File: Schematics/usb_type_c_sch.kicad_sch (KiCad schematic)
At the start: 4 parts, among them J3 USB_C_Receptacle

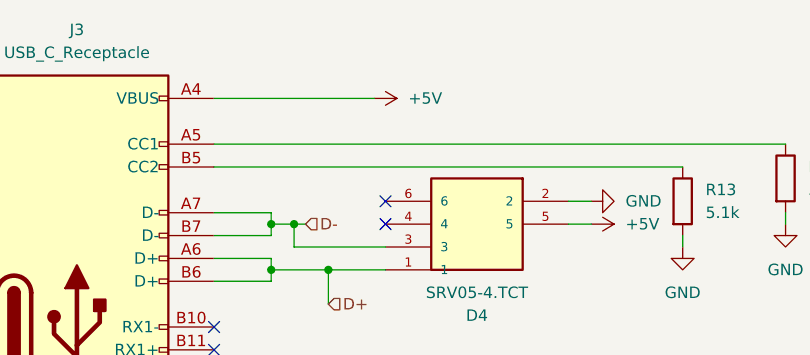
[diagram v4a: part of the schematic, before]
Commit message: finished pin assignments and ran ERC all good ready for layout
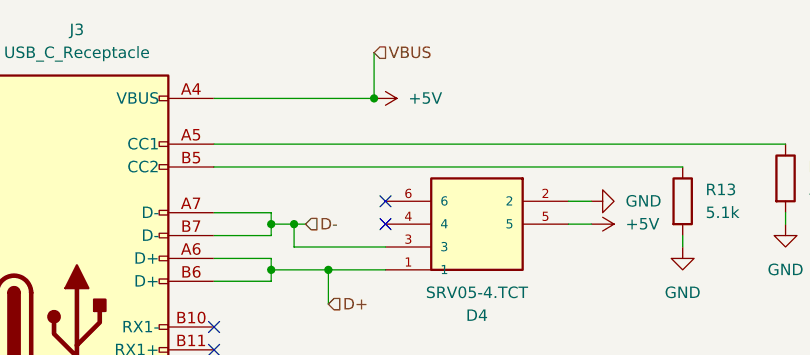
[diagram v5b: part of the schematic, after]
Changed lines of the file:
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@@
+	)
+	(junction
+		(at 140.97 57.15)
+		(diameter 0)
+		(color 0 0 0 0)
 	)
 	(junction
@@
 		(pts
 			(xy 104.14 124.46) (xy 107.95 124.46)
+		)
+		(stroke
+			(width 0)
+			(type default)
+		)
+	)
+	(wire
+		(pts
+			(xy 140.97 52.07) (xy 140.97 57.15)
 		)
 		(stroke
@@
 		(shape input)
 		(at 135.89 80.01 0)
+		(effects
+			(font
+				(size 1.27 1.27)
+			)
+			(justify left)
+		)
+	)
+	(hierarchical_label "VBUS"
+		(shape input)
+		(at 140.97 52.07 0)
 		(effects
 			(font
@@
 			)
 		)
+		(property "Description_1" ""
+			(at 107.95 82.55 0)
+			(effects
+				(font
+					(size 1.27 1.27)
+				)
+				(hide yes)
+			)
+		)
+		(property "MF" ""
+			(at 107.95 82.55 0)
+			(effects
+				(font
+					(size 1.27 1.27)
+				)
+				(hide yes)
+			)
+		)
+		(property "MP" ""
+			(at 107.95 82.55 0)
+			(effects
+				(font
+					(size 1.27 1.27)
+				)
+				(hide yes)
+			)
+		)
+		(property "Package" ""
+			(at 107.95 82.55 0)
+			(effects
+				(font
+					(size 1.27 1.27)
+				)
+				(hide yes)
+			)
+		)
+		(property "Price" ""
+			(at 107.95 82.55 0)
+			(effects
+				(font
+					(size 1.27 1.27)
+				)
+				(hide yes)
+			)
+		)
+		(property "Purchase-URL" ""
+			(at 107.95 82.55 0)
+			(effects
+				(font
+					(size 1.27 1.27)
+				)
+				(hide yes)
+			)
+		)
 		(pin "S1"
 		)
@@
 			)
 		)
+		(property "Description_1" ""
+			(at 162.56 73.66 0)
+			(effects
+				(font
+					(size 1.27 1.27)
+				)
+				(hide yes)
+			)
+		)
+		(property "MF" ""
+			(at 162.56 73.66 0)
+			(effects
+				(font
+					(size 1.27 1.27)
+				)
+				(hide yes)
+			)
+		)
+		(property "MP" ""
+			(at 162.56 73.66 0)
+			(effects
+				(font
+					(size 1.27 1.27)
+				)
+				(hide yes)
+			)
+		)
+		(property "Package" ""
+			(at 162.56 73.66 0)
+			(effects
+				(font
+					(size 1.27 1.27)
+				)
+				(hide yes)
+			)
+		)
+		(property "Price" ""
+			(at 162.56 73.66 0)
+			(effects
+				(font
+					(size 1.27 1.27)
+				)
+				(hide yes)
+			)
+		)
+		(property "Purchase-URL" ""
+			(at 162.56 73.66 0)
+			(effects
+				(font
+					(size 1.27 1.27)
+				)
+				(hide yes)
+			)
+		)
 		(pin "4"
 		)
@@
 			)
 		)
+		(property "Description_1" ""
+			(at 186.69 66.04 0)
+			(effects
+				(font
+					(size 1.27 1.27)
+				)
+				(hide yes)
+			)
+		)
+		(property "MF" ""
+			(at 186.69 66.04 0)
+			(effects
+				(font
+					(size 1.27 1.27)
+				)
+				(hide yes)
+			)
+		)
+		(property "MP" ""
+			(at 186.69 66.04 0)
+			(effects
+				(font
+					(size 1.27 1.27)
+				)
+				(hide yes)
+			)
+		)
+		(property "Package" ""
+			(at 186.69 66.04 0)
+			(effects
+				(font
+					(size 1.27 1.27)
+				)
+				(hide yes)
+			)
+		)
+		(property "Price" ""
+			(at 186.69 66.04 0)
+			(effects
+				(font
+					(size 1.27 1.27)
+				)
+				(hide yes)
+			)
+		)
+		(property "Purchase-URL" ""
+			(at 186.69 66.04 0)
+			(effects
+				(font
+					(size 1.27 1.27)
+				)
+				(hide yes)
+			)
+		)
 		(pin "2"
 		)
@@
 			(at 175.26 68.58 0)
 			(effects
+				(font
+					(size 1.27 1.27)
+				)
+				(hide yes)
+			)
+		)
+		(property "Description_1" ""
+			(at 175.26 68.58 0)
+			(effects
+				(font
+					(size 1.27 1.27)
+				)
+				(hide yes)
+			)
+		)
+		(property "MF" ""
+			(at 175.26 68.58 0)
+			(effects
+				(font
+					(size 1.27 1.27)
+				)
+				(hide yes)
+			)
+		)
+		(property "MP" ""
+			(at 175.26 68.58 0)
+			(effects
+				(font
+					(size 1.27 1.27)
+				)
+				(hide yes)
+			)
+		)
+		(property "Package" ""
+			(at 175.26 68.58 0)
+			(effects
+				(font
+					(size 1.27 1.27)
+				)
+				(hide yes)
+			)
+		)
+		(property "Price" ""
+			(at 175.26 68.58 0)
+			(effects
+				(font
+					(size 1.27 1.27)
+				)
+				(hide yes)
+			)
+		)
+		(property "Purchase-URL" ""
+			(at 175.26 68.58 0)
+			(effects

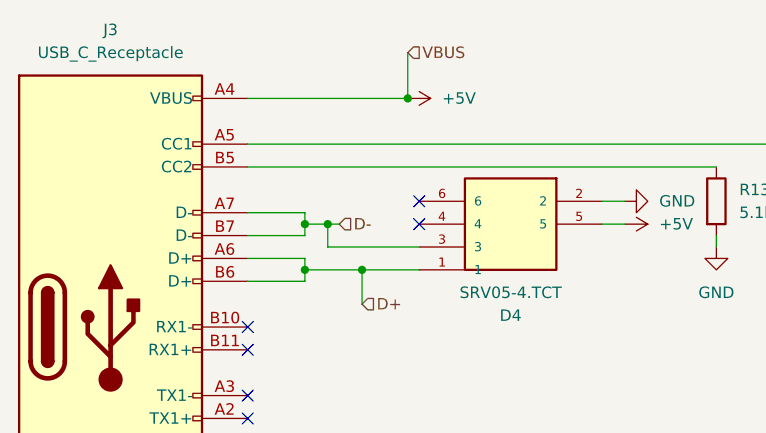
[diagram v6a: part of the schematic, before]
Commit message: began routing, need layout approval
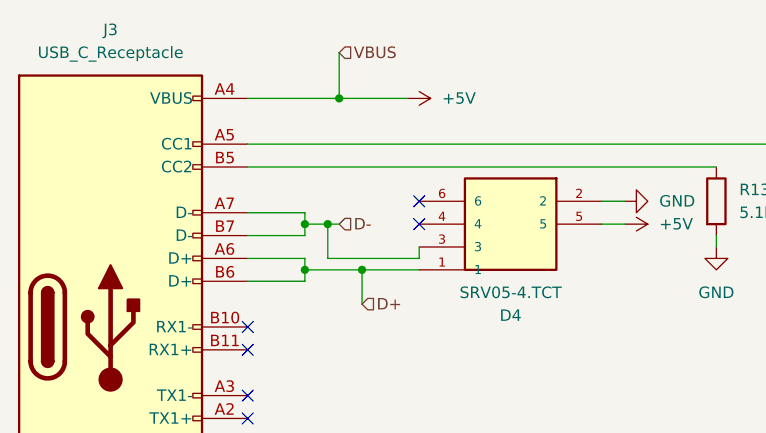
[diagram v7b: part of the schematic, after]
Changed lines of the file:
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@@
 	(paper "A4")
 	(junction
+		(at 133.35 57.15)
+		(diameter 0)
+		(color 0 0 0 0)
+	)
+	(junction
 		(at 129.54 71.12)
 		(diameter 0)
@@
 	)
 	(junction
-		(at 140.97 57.15)
-		(diameter 0)
-		(color 0 0 0 0)
-	)
-	(junction
 		(at 104.14 124.46)
 		(diameter 0)
@@
 	(wire
 		(pts
+			(xy 133.35 57.15) (xy 140.97 57.15)
+		)
+		(stroke
+			(width 0)
+			(type default)
+		)
+	)
+	(wire
+		(pts
+			(xy 132.08 74.93) (xy 142.24 74.93)
+		)
+		(stroke
+			(width 0)
+			(type default)
+		)
+	)
+	(wire
+		(pts
 			(xy 104.14 124.46) (xy 104.14 128.27)
 		)
@@
 	(wire
 		(pts
+			(xy 135.89 76.2) (xy 142.24 76.2)
+		)
+		(stroke
+			(width 0)
+			(type default)
+		)
+	)
+	(wire
+		(pts
 			(xy 129.54 69.85) (xy 129.54 71.12)
 		)
@@
 	(wire
 		(pts
-			(xy 132.08 71.12) (xy 132.08 73.66)
+			(xy 132.08 71.12) (xy 132.08 74.93)
 		)
 		(stroke
@@
 	(wire
 		(pts
+			(xy 142.24 74.93) (xy 142.24 73.66)
+		)
+		(stroke
+			(width 0)
+			(type default)
+		)
+	)
+	(wire
+		(pts
 			(xy 129.54 71.12) (xy 132.08 71.12)
 		)
@@
 	(wire
 		(pts
-			(xy 135.89 76.2) (xy 142.24 76.2)
-		)
-		(stroke
-			(width 0)
-			(type default)
-		)
-	)
-	(wire
-		(pts
 			(xy 100.33 124.46) (xy 104.14 124.46)
 		)
@@
 	(wire
 		(pts
-			(xy 132.08 73.66) (xy 142.24 73.66)
-		)
-		(stroke
-			(width 0)
-			(type default)
-		)
-	)
-	(wire
-		(pts
 			(xy 129.54 71.12) (xy 129.54 72.39)
 		)
@@
 	(wire
 		(pts
-			(xy 140.97 52.07) (xy 140.97 57.15)
+			(xy 133.35 52.07) (xy 133.35 57.15)
 		)
 		(stroke
@@
 	(wire
 		(pts
-			(xy 123.19 57.15) (xy 140.97 57.15)
+			(xy 123.19 57.15) (xy 133.35 57.15)
 		)
 		(stroke
@@
 	(hierarchical_label "VBUS"
 		(shape input)
-		(at 140.97 52.07 0)
+		(at 133.35 52.07 0)
 		(effects
 			(font

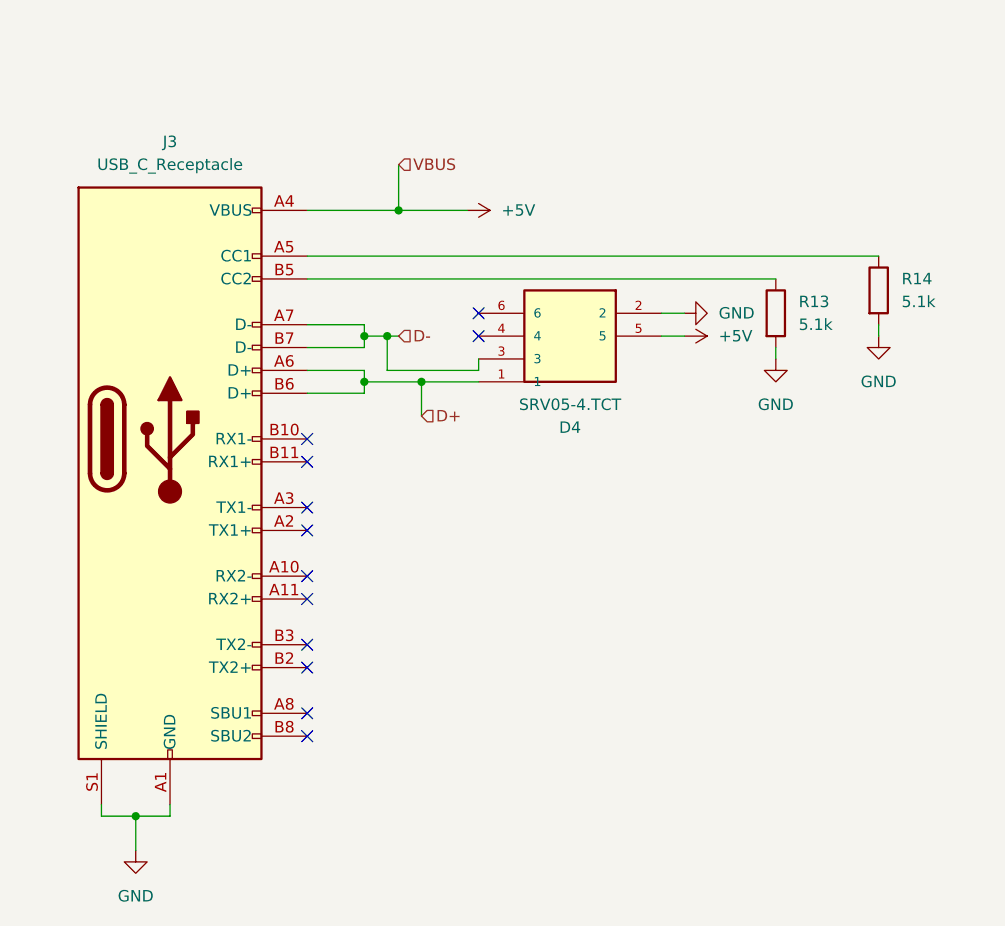
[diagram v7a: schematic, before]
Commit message: fixing DRC Warnings updated USBC footprint/schematic, did impedance matching for the trace from rfm95 to antenna connector fixed resistor on flash memeory
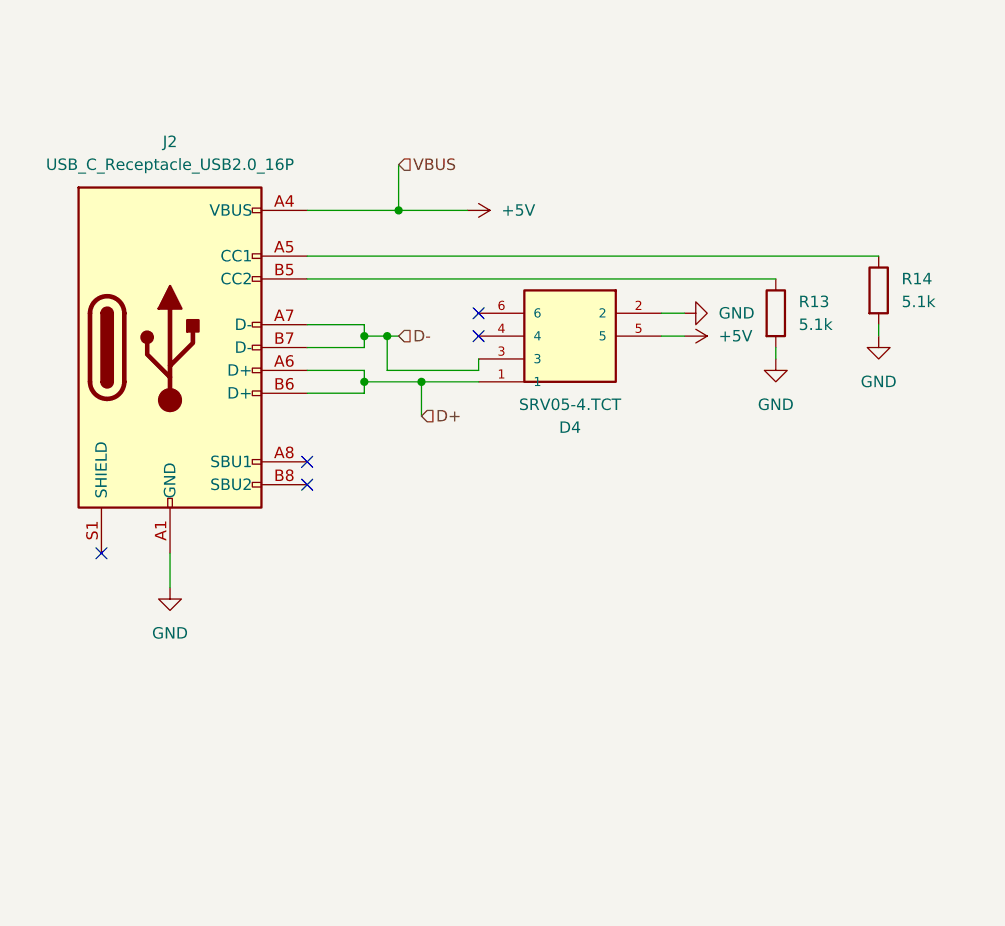
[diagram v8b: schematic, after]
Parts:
- removed J3: USB_C_Receptacle, Library:HRO_TYPE-C-31-M-12, symbol Connector:USB_C_Receptacle
- added J2: USB_C_Receptacle_USB2.0_16P, Connector_USB:USB_C_Receptacle_HRO_TYPE-C-31-M-12, symbol Connector:USB_C_Receptacle_USB2.0_16P
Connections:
- net +5V: now also J2.A4 (VBUS), J2.A9 (VBUS), J2.B4 (VBUS), J2.B9 (VBUS)
- net D+: now also J2.A6 (D+), J2.B6 (D+)
- net D-: now also J2.A7 (D-), J2.B7 (D-)
- net GND: now also J2.A1 (GND), J2.A12 (GND), J2.B1 (GND), J2.B12 (GND)
- net at R14.1: now also J2.A5 (CC1)
- net at R13.1: now also J2.B5 (CC2)
- no-connect marks 12 -> 5
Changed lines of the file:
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@@
 		(color 0 0 0 0)
-	)
-	(junction
-		(at 104.14 124.46)
-		(diameter 0)
-		(color 0 0 0 0)
-	)
-	(no_connect
-		(at 123.19 105.41)
 	)
 	(no_connect
@@
 	)
 	(no_connect
-		(at 123.19 113.03)
+		(at 123.19 85.09)
 	)
 	(no_connect
-		(at 123.19 85.09)
+		(at 100.33 95.25)
 	)
 	(no_connect
-		(at 123.19 82.55)
-	)
-	(no_connect
-		(at 123.19 92.71)
-	)
-	(no_connect
-		(at 123.19 107.95)
-	)
-	(no_connect
-		(at 123.19 115.57)
-	)
-	(no_connect
-		(at 123.19 97.79)
-	)
-	(no_connect
-		(at 123.19 100.33)
-	)
-	(no_connect
-		(at 123.19 90.17)
+		(at 123.19 87.63)
 	)
 	(wire
@@
 	(wire
 		(pts
-			(xy 107.95 124.46) (xy 107.95 123.19)
-		)
-		(stroke
-			(width 0)
-			(type default)
-		)
-	)
-	(wire
-		(pts
 			(xy 135.89 80.01) (xy 135.89 76.2)
 		)
@@
 	(wire
 		(pts
-			(xy 104.14 124.46) (xy 104.14 128.27)
+			(xy 107.95 95.25) (xy 107.95 99.06)
 		)
 		(stroke
@@
 	(wire
 		(pts
-			(xy 100.33 124.46) (xy 104.14 124.46)
-		)
-		(stroke
-			(width 0)
-			(type default)
-		)
-	)
-	(wire
-		(pts
 			(xy 129.54 71.12) (xy 129.54 72.39)
 		)
@@
 	(wire
 		(pts
-			(xy 104.14 124.46) (xy 107.95 124.46)
-		)
-		(stroke
-			(width 0)
-			(type default)
-		)
-	)
-	(wire
-		(pts
 			(xy 133.35 52.07) (xy 133.35 57.15)
 		)
@@
 		(pts
 			(xy 123.19 57.15) (xy 133.35 57.15)
-		)
-		(stroke
-			(width 0)
-			(type default)
-		)
-	)
-	(wire
-		(pts
-			(xy 100.33 124.46) (xy 100.33 123.19)
 		)
 		(stroke
@@
 			)
 			(justify left)
-		)
-	)
-	(symbol
-		(lib_id "Connector:USB_C_Receptacle")
-		(at 107.95 82.55 0)
-		(unit 1)
-		(exclude_from_sim no)
-		(in_bom yes)
-		(on_board yes)
-		(dnp no)
-		(fields_autoplaced yes)
-		(property "Reference" "J3"
-			(at 107.95 49.53 0)
-			(effects
-				(font
-					(size 1.27 1.27)
-				)
-			)
-		)
-		(property "Value" "USB_C_Receptacle"
-			(at 107.95 52.07 0)
-			(effects
-				(font
-					(size 1.27 1.27)
-				)
-			)
-		)
-		(property "Footprint" "Library:HRO_TYPE-C-31-M-12"
-			(at 111.76 82.55 0)
-			(effects
-				(font
-					(size 1.27 1.27)
-				)
-				(hide yes)
-			)
-		)
-		(property "Datasheet" "https://www.usb.org/sites/default/files/documents/usb_type-c.zip"
-			(at 111.76 82.55 0)
-			(effects
-				(font
-					(size 1.27 1.27)
-				)
-				(hide yes)
-			)
-		)
-		(property "Description" "USB Full-Featured Type-C Receptacle connector"
-			(at 107.95 82.55 0)
-			(effects
-				(font
-					(size 1.27 1.27)
-				)
-				(hide yes)
-			)
-		)
-		(property "LCSC Part" "C49566391"
-			(at 107.95 82.55 0)
-			(effects
-				(font
-					(size 1.27 1.27)
-				)
-				(hide yes)
-			)
-		)
-		(property "Description_1" ""
-			(at 107.95 82.55 0)
-			(effects
-				(font
-					(size 1.27 1.27)
-				)
-				(hide yes)
-			)
-		)
-		(property "MF" ""
-			(at 107.95 82.55 0)
-			(effects
-				(font
-					(size 1.27 1.27)
-				)
-				(hide yes)
-			)
-		)
-		(property "MP" ""
-			(at 107.95 82.55 0)
-			(effects
-				(font
-					(size 1.27 1.27)
-				)
-				(hide yes)
-			)
-		)
-		(property "Package" ""
-			(at 107.95 82.55 0)
-			(effects
-				(font
-					(size 1.27 1.27)
-				)
-				(hide yes)
-			)
-		)
-		(property "Price" ""
-			(at 107.95 82.55 0)
-			(effects
-				(font
-					(size 1.27 1.27)
-				)
-				(hide yes)
-			)
-		)
-		(property "Purchase-URL" ""
-			(at 107.95 82.55 0)
-			(effects
-				(font
-					(size 1.27 1.27)
-				)
-				(hide yes)
-			)
-		)
-		(pin "S1"
-		)
-		(pin "A12"
-		)
-		(pin "A9"
-		)
-		(pin "A5"
-		)
-		(pin "A7"
-		)
-		(pin "B4"
-		)
-		(pin "A1"
-		)
-		(pin "B1"
-		)
-		(pin "B12"
-		)
-		(pin "A4"
-		)
-		(pin "B9"
-		)
-		(pin "B5"
-		)
-		(pin "A3"
-		)
-		(pin "B7"
-		)
-		(pin "A10"
-		)
-		(pin "A11"
-		)
-		(pin "A6"
-		)
-		(pin "B11"
-		)
-		(pin "B2"
-		)
-		(pin "B8"
-		)
-		(pin "B3"
-		)
-		(pin "B6"
-		)
-		(pin "A2"
-		)
-		(pin "B10"
-		)
-		(pin "A8"
-		)
-		(instances
-			(project "flightcomputer2"
-				(path "/6cb3dda3-5fe8-4715-b831-354360aa3199/105f27ec-5fab-44f4-a683-69b23a7486f0"
-					(reference "J3")
-					(unit 1)
-				)
-			)
 		)
 	)
@@
 	(symbol
 		(lib_id "power:GND")
-		(at 104.14 128.27 0)
+		(at 107.95 99.06 0)
 		(unit 1)
 		(exclude_from_sim no)
@@
 		(fields_autoplaced yes)
 		(property "Reference" "#PWR051"
-			(at 104.14 134.62 0)
+			(at 107.95 105.41 0)
 			(effects
 				(font
@@
 		)
 		(property "Value" "GND"
-			(at 104.14 133.35 0)
+			(at 107.95 104.14 0)
 			(effects
 				(font
@@
 		)
 		(property "Footprint" ""
-			(at 104.14 128.27 0)
+			(at 107.95 99.06 0)
 			(effects
 				(font
@@
 		)
 		(property "Datasheet" ""
-			(at 104.14 128.27 0)
+			(at 107.95 99.06 0)
 			(effects
 				(font
@@
 		)
 		(property "Description" "Power symbol creates a global label with name \"GND\" , ground"
-			(at 104.14 128.27 0)
+			(at 107.95 99.06 0)
 			(effects
 				(font
@@
 					(unit 1)
 				)
+			)
+		)
+	)
+	(symbol
+		(lib_id "Connector:USB_C_Receptacle_USB2.0_16P")
+		(at 107.95 72.39 0)
+		(unit 1)
+		(exclude_from_sim no)
+		(in_bom yes)
+		(on_board yes)
+		(dnp no)
+		(fields_autoplaced yes)
+		(property "Reference" "J2"
+			(at 107.95 49.53 0)
+			(effects
+				(font
+					(size 1.27 1.27)
+				)
+			)
+		)
+		(property "Value" "USB_C_Receptacle_USB2.0_16P"
+			(at 107.95 52.07 0)
+			(effects
+				(font
+					(size 1.27 1.27)
+				)
+			)
+		)
+		(property "Footprint" "Connector_USB:USB_C_Receptacle_HRO_TYPE-C-31-M-12"
+			(at 111.76 72.39 0)
+			(effects
+				(font
+					(size 1.27 1.27)
+				)
+				(hide yes)
+			)
+		)
+		(property "Datasheet" "https://www.usb.org/sites/default/files/documents/usb_type-c.zip"
+			(at 111.76 72.39 0)
+			(effects
+				(font
+					(size 1.27 1.27)
+				)
+				(hide yes)
+			)
+		)
+		(property "Description" "USB 2.0-only 16P Type-C Receptacle connector"
+			(at 107.95 72.39 0)
+			(effects
+				(font
+					(size 1.27 1.27)
+				)
+				(hide yes)
+			)
+		)
+		(pin "A5"
+		)
+		(pin "A7"
+		)
+		(pin "B9"
+		)
+		(pin "A6"
+		)
+		(pin "A12"
+		)
+		(pin "A9"
+		)
+		(pin "B6"
+		)
+		(pin "B12"
+		)
+		(pin "A1"
+		)
+		(pin "S1"
+		)
+		(pin "B1"
+		)
+		(pin "B8"
+		)
+		(pin "A8"
+		)
+		(pin "B5"
+		)
+		(pin "A4"
+		)
+		(pin "B4"
+		)
+		(pin "B7"
+		)
+		(instances
+			(project ""
+				(path "/6cb3dda3-5fe8-4715-b831-354360aa3199/105f27ec-5fab-44f4-a683-69b23a7486f0"
+					(reference "J2")
+					(unit 1)
+				)
